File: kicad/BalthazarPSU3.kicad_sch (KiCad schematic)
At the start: 86 parts

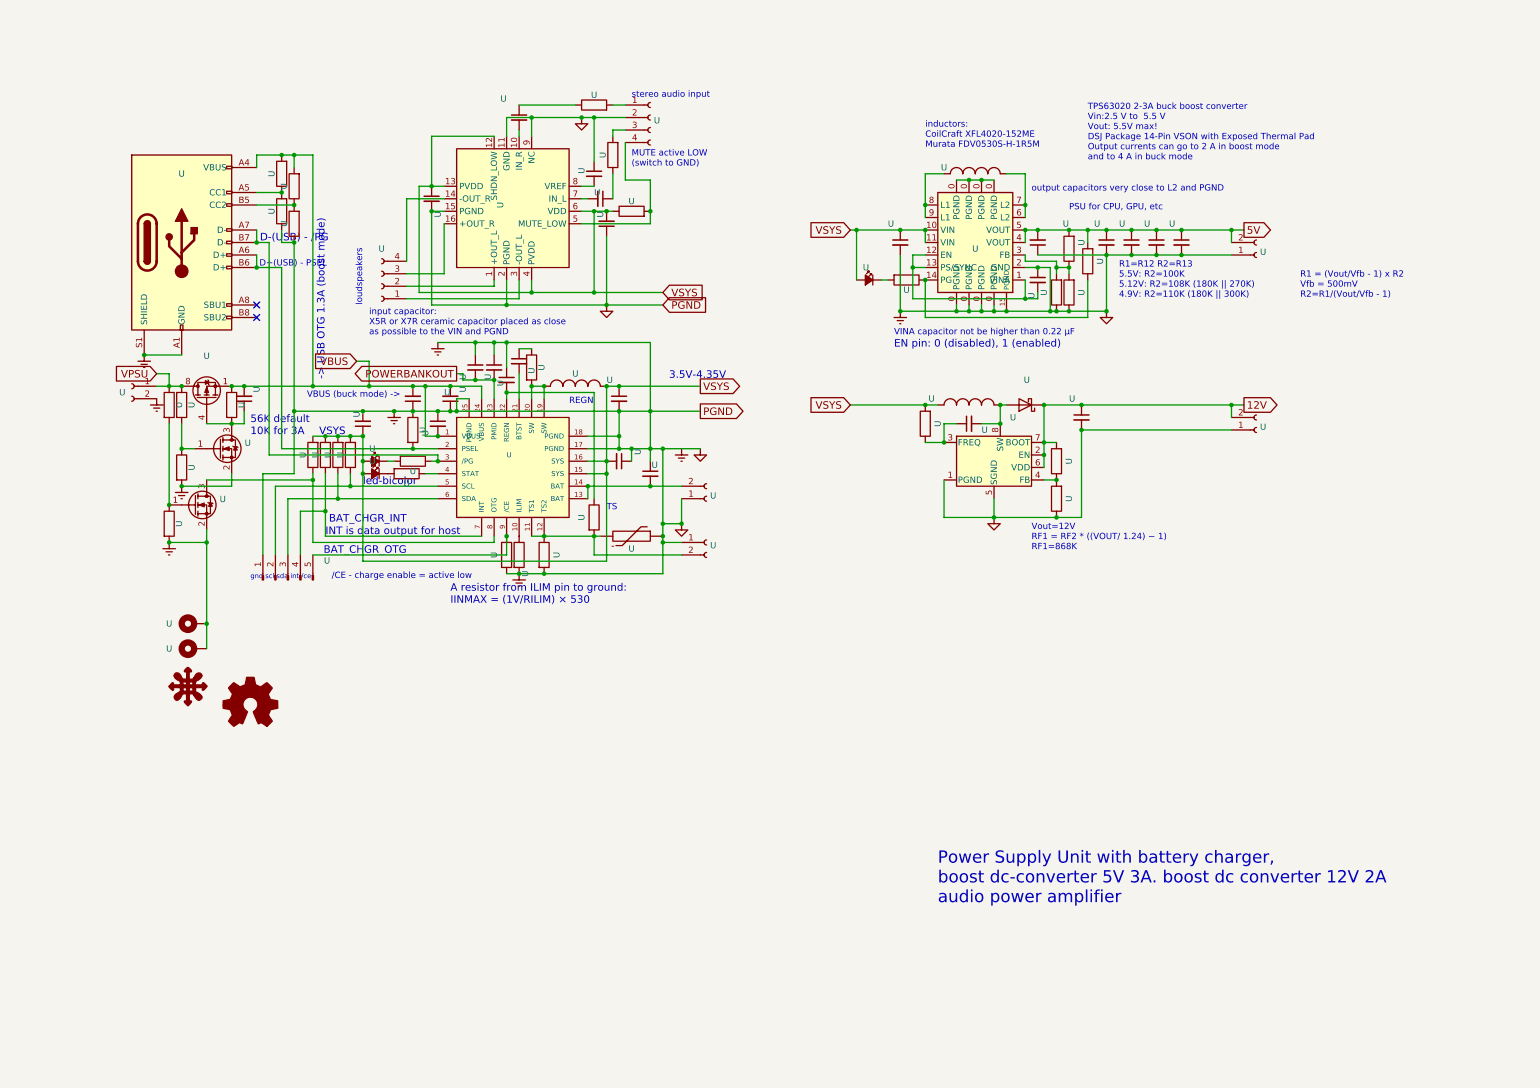
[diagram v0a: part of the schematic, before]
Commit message: Adding new symbol and footprint for U2
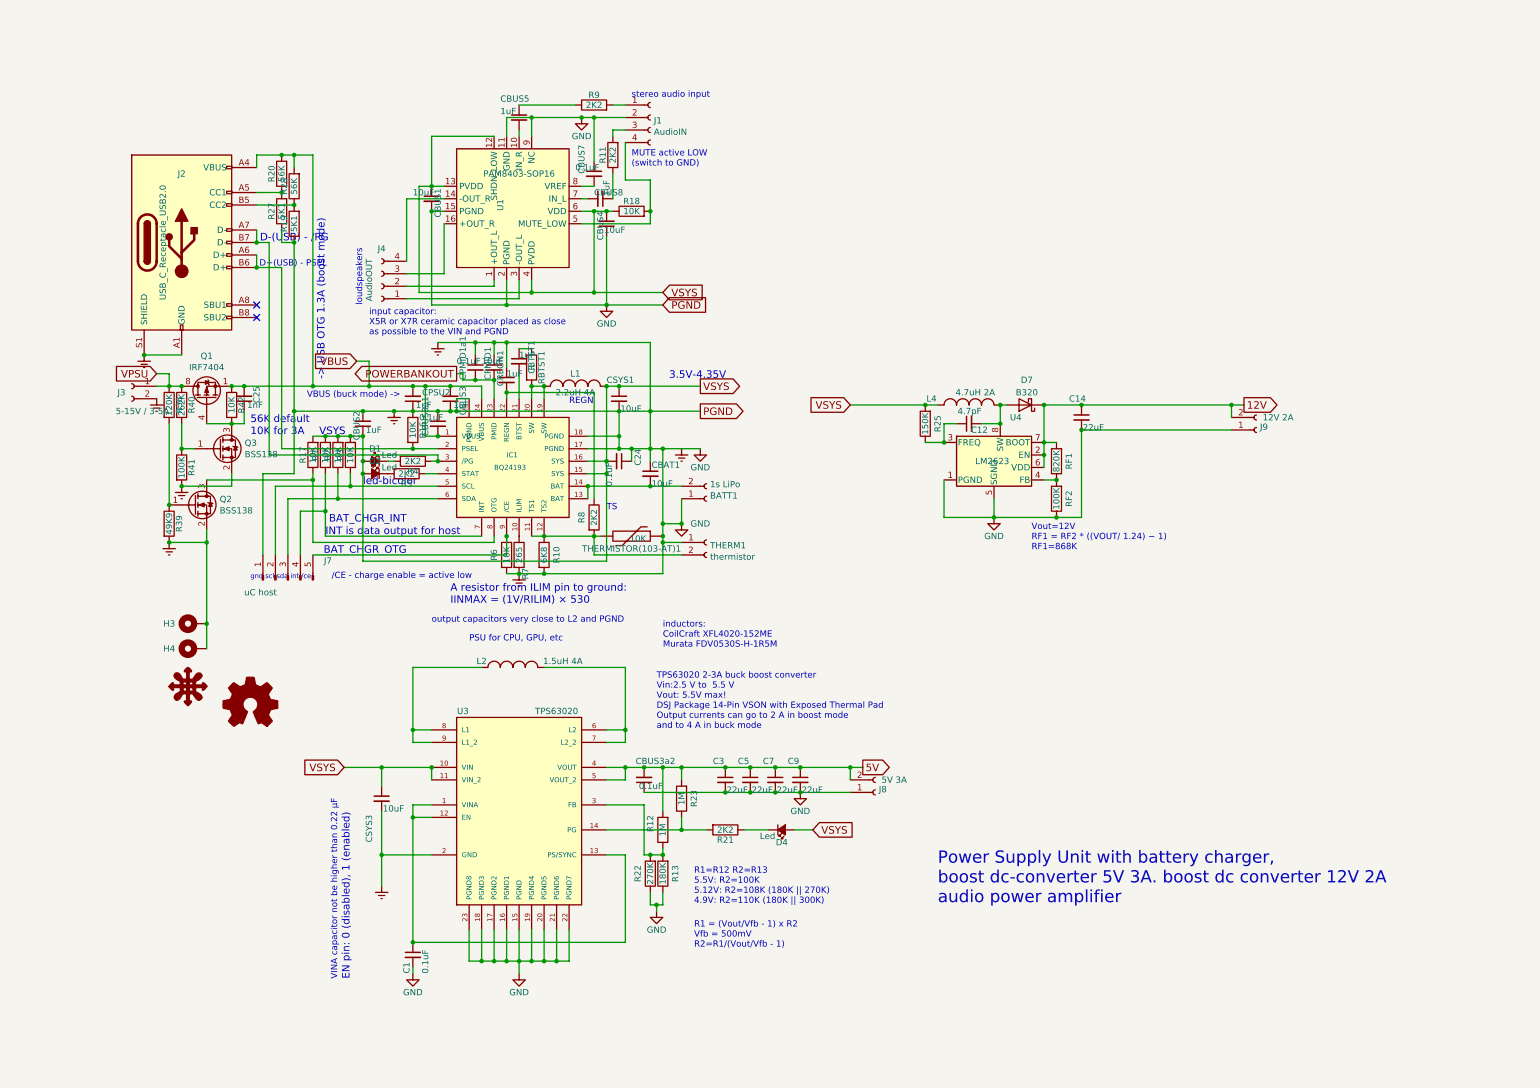
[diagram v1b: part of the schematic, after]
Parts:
- removed U: (no value), symbol BalthazarPSU2-rescue:TPS63020-Regulator_Switching
- removed U: (no value), symbol BalthazarPSU2-rescue:BALTHAZA_LOGO_SMALL-Graphic
- removed U: (no value), symbol Graphic:Logo_Open_Hardware_Small
- added U3: TPS63020, QFN14-3X4MM, symbol TPS63020:TPS63020
- BATT1: renamed from U; value (none) -> 1s LiPo; footprint (none) -> TerminalBlock:TerminalBlock_bornier-2_P5.08mm
- C1, C24, CBUS3a1, CBUS3a2, CBUS7, CPMID1a1: renamed from U; value (none) -> 0.1uF; footprint (none) -> Capacitor_SMD:C_0805_2012Metric
- C12: renamed from U; value (none) -> 4.7pF; footprint (none) -> Capacitor_SMD:C_0805_2012Metric
- C14, C3, C5, C7, C9: renamed from U; value (none) -> 22uF; footprint (none) -> Capacitor_SMD:C_1206_3216Metric
- C25: renamed from U; value (none) -> 1nF; footprint (none) -> Capacitor_SMD:C_0805_2012Metric
- CBAT1, CBUS1, CBUS4, CPMID1, CSYS1, CSYS3: renamed from U; value (none) -> 10uF; footprint (none) -> Capacitor_SMD:C_1206_3216Metric
- CBTST1, CBUS2, CBUS3, CBUS5, CBUS8, CPSU2, CREGN1: renamed from U; value (none) -> 1uF; footprint (none) -> Capacitor_SMD:C_1206_3216Metric
- D1, D2, D4: renamed from U; value (none) -> Led; footprint (none) -> LED_SMD:LED_1206_3216Metric
- D7: renamed from U; value (none) -> B320; footprint (none) -> Diode_SMD:D_SMB
- H3: renamed from U; value (none) -> hole; footprint (none) -> MountingHole:MountingHole_2.2mm_M2_Pad
- H4: renamed from U; value (none) -> MountingHole_Pad; footprint (none) -> MountingHole:MountingHole_2.2mm_M2_Pad
- IC1: renamed from U; value (none) -> BQ24193; footprint (none) -> Package_DFN_QFN:QFN-24-1EP_4x4mm_P0.5mm_EP2.7x2.7mm_ThermalVias
- J1: renamed from U; value (none) -> AudioIN; footprint (none) -> Connector_PinSocket_2.00mm:PinSocket_1x04_P2.00mm_Vertical
- J2: renamed from U; value (none) -> USB_C_Receptacle_USB2.0; footprint (none) -> Connector_USB:USB_C_Receptacle_GCT_USB4085
- J3: renamed from U; value (none) -> 5-15V / 3-5A; footprint (none) -> Connector_BarrelJack:BarrelJack_Horizontal
- J4: renamed from U; value (none) -> AudioOUT; footprint (none) -> Connector_PinSocket_2.54mm:PinSocket_1x04_P2.54mm_Vertical
- J7: renamed from U; value (none) -> uC host; footprint (none) -> Connector_PinSocket_2.00mm:PinSocket_1x05_P2.00mm_Vertical
- J8: renamed from U; value (none) -> 5V 3A; footprint (none) -> TerminalBlock:TerminalBlock_bornier-2_P5.08mm
- J9: renamed from U; value (none) -> 12V 2A; footprint (none) -> TerminalBlock:TerminalBlock_bornier-2_P5.08mm
- L1: renamed from U; value (none) -> 2.2uH 4A; footprint (none) -> Inductor_SMD:L_Bourns_SRP7028A_7.3x6.6mm
- L2: renamed from U; value (none) -> 1.5uH 4A; footprint (none) -> Inductor_SMD:L_Bourns_SRP7028A_7.3x6.6mm
- L4: renamed from U; value (none) -> 4.7uH 2A; footprint (none) -> Inductor_SMD:L_Bourns_SRP5030T
- Q1: renamed from U; value (none) -> IRF7404; footprint (none) -> Package_SO:SOIC-8_3.9x4.9mm_P1.27mm
- Q2, Q3: renamed from U; value (none) -> BSS138; footprint (none) -> Package_TO_SOT_SMD:SOT-23
- R1, R16, R17, R18, R2, R3, R42, R6, THERMISTOR(103-AT)1: renamed from U; value (none) -> 10K; footprint (none) -> Resistor_SMD:R_0805_2012Metric
- R10: renamed from U; value (none) -> 6K8; footprint (none) -> Resistor_SMD:R_0805_2012Metric
- R11, R21, R4, R5, R8, R9: renamed from U; value (none) -> 2K2; footprint (none) -> Resistor_SMD:R_0805_2012Metric
- R12, R23: renamed from U; value (none) -> 1M; footprint (none) -> Resistor_SMD:R_0805_2012Metric
- R13: renamed from U; value (none) -> 180K; footprint (none) -> Resistor_SMD:R_0805_2012Metric
- R19, R27: renamed from U; value (none) -> 5K1; footprint (none) -> Resistor_SMD:R_0805_2012Metric
- R20, R28: renamed from U; value (none) -> 56K; footprint (none) -> Resistor_SMD:R_0805_2012Metric
- R22: renamed from U; value (none) -> 270K; footprint (none) -> Resistor_SMD:R_0805_2012Metric
- R25: renamed from U; value (none) -> 150K; footprint (none) -> Resistor_SMD:R_0805_2012Metric
- R38: renamed from U; value (none) -> 120K; footprint (none) -> Resistor_SMD:R_1206_3216Metric
- R39: renamed from U; value (none) -> 49K9; footprint (none) -> Resistor_SMD:R_1206_3216Metric
- R40: renamed from U; value (none) -> 262K; footprint (none) -> Resistor_SMD:R_0805_2012Metric
- R41, RF2: renamed from U; value (none) -> 100K; footprint (none) -> Resistor_SMD:R_0805_2012Metric
- R7: renamed from U; value (none) -> 265; footprint (none) -> Resistor_SMD:R_0805_2012Metric
- RBTST1: renamed from U; value (none) -> R; footprint (none) -> Resistor_SMD:R_0805_2012Metric
- RF1: renamed from U; value (none) -> 820K; footprint (none) -> Resistor_SMD:R_0805_2012Metric
- THERM1: renamed from U; value (none) -> thermistor; footprint (none) -> TestPoint:TestPoint_2Pads_Pitch2.54mm_Drill0.8mm
- U1: renamed from U; value (none) -> PAM8403-SOP16; footprint (none) -> Package_SO:SOP-16_4.4x10.4mm_P1.27mm
- U4: renamed from U; value (none) -> LM2623; footprint (none) -> Package_SO:VSSOP-8_3.0x3.0mm_P0.65mm
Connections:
- net 5V: now also U3.4 (VOUT), U3.5 (VOUT_2)
- net Earth: now also C1.2, U3.15 (PGND), U3.16 (PGND1), U3.17 (PGND2), U3.18 (PGND3), U3.19 (PGND4), U3.2 (GND), U3.20 (PGND5), U3.21 (PGND6), U3.22 (PGND7), U3.23 (PGND8); no longer C1.1
- net VSYS: now also U3.10 (VIN), U3.11 (VIN_2)
- net at R23.1: now also R21.2, U3.14 (PG); no longer R21.1
- net at D4.2 (C): now also R21.1; no longer R21.2
- net at R12.1, R13.2, R22.2: now also U3.3 (FB)
- net at L2.2: now also U3.6 (L2), U3.7 (L2_2)
- net at L2.1: now also U3.8 (L1), U3.9 (L1_2)
- new net: C1.1, U3.1 (VINA), U3.12 (EN), U3.13 (PS/SYNC)
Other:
- moved on the sheet: C1, C3, C5, C7, C9, CBUS3a2, CSYS3, D4, J8, L2, R12, R13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

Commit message: Adding info fix #9
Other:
- company: (none) ->  Balthazar Foundation 
- title: (none) -> Balthazar PSU
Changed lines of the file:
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@@
 (kicad_sch (version 20221004) (generator eeschema)
   (paper "A4")
+  (title_block
+    (title "Balthazar PSU")
+    (date "2022-10-11")
+    (rev "v02")
+    (company " Balthazar Foundation ")
+    (comment 1 "License: CERN-OHL-S")
+  )
   (junction (at 31.75 121.92) (diameter 0) (color 0 0 0 0)
   )
